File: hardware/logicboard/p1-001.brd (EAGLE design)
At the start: 91 x 90 mm, 70 parts, among them IC1 74LS06N, IC2 4066N, J1 MKR, J2 GPIO, J3 Vcc, J4 RLY, J42 RLY2, J5 SPI, J6 LED, J7 DIN5, J8 DIN5, J9 DIN5, K1 G5V1, Q1 220mA/50V/3.5Ω, Q2 220mA/50V/3.5Ω, T1 2SC1815, U1 DS18B20

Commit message: Removed many parts.
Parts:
- removed A, B: (no value), wirepad:SMD1,27-2,54
- removed C1: 22u, rcl:C025-050X050
- removed C11, C4: 100n, rcl:C025-024X044
- removed C12, C13, C3: 1u, rcl:C050-024X044
- removed C2: 470n, rcl:C050-024X044
- removed D1: (no value), SparkFun-DiscreteSemi:DIODE-1N4148
- removed F1: 1.8A, fuse:TE5
- removed H1, H2: STAND-OFF, SparkFun-Hardware:STAND-OFF
- removed IC1: 74LS06N, 74xx-us:DIL14
- removed IC2: 4066N, 40xx:DIL14
- removed J1: MKR, SparkFun-Connectors:JST-5-PTH
- removed J2: GPIO, SparkFun-Connectors:JST-3-PTH
- removed J3: Vcc, SparkFun-Connectors:JST-2-PTH
- removed J4: RLY, SparkFun-Connectors:JST-2-SMD
- removed J5: SPI, SparkFun-Connectors:JST-5-PTH-VERT
- removed J8, J9: DIN5, SparkFun-Connectors:DIN5-RA-PTH
- removed JP1: PWRSEL, pinhead:2X03
- removed JP2: RTC, SparkFun-Connectors:1X05
- removed JP4: RLYJMP, pinhead:1X02
- removed JP5: PWR, pinhead:1X03
- removed JP7: MNTR, pinhead:1X04
- removed LCD1: AQM0802A-RN-GBW, AQM0802A-RN-GBW:AQM0802A-RN-GBW-FOOTPRINT
- removed Q1, Q2: 220mA/50V/3.5Ω, SparkFun-DiscreteSemi:SOT23-3
- removed R101, R102, R103, R104: 10k, rcl:M2012
- removed RN1: 10k, resistor-net:RN-5
- removed RZ1**, RZ2**, VCCBRIDGE**: Inf, rcl:M2012
- removed SV1: (no value), con-ml:ML16L
- removed U1: DS18B20, SparkFun-Sensors:TO-92-AMMO
- removed V1: 5V, v-reg:78XXL
- removed VDDBRIDGE: 0, rcl:M2012
- moved SV3 13.0 mm to (55.5, 11.0)
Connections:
- removed net ANLG0R: IC2.2, SV1.3
- removed net ANLG1R: IC2.3, SV1.7
- removed net ANLG2R: IC2.9, SV1.11
- removed net ANLG3R: IC2.10, SV1.15
- removed net CAP1N: C12.2, LCD1.3
- removed net CAP1P: C12.1, LCD1.4
- removed net LCDVOUT: C13.2, LCD1.2
- removed net MO2RTN: RN4.9
- removed net MO2SND: RN4.10
- removed net MORTN: J9.5, RN4.13
- removed net MOSND: J9.4, RN4.14
- removed net MTRTN: J8.5, RN4.11
- removed net MTSND: J8.4, RN4.12
- removed net N$1: IC1.8, RN4.6
- removed net N$2: IC1.10, RN4.4
- removed net N$6: IC1.12, RN4.8
- removed net RLYOUT: J4.2, J42.1, K1.10
- removed net SCL: J1.3, Q1.3, R101.1, RZ1**.1
- removed net SDA3V: LCD1.7, Q2.2, R104.1, RZ2**.2
- removed net V+: C1.1, C2.1, D1.C, J0.3, JP1.1, JP5.3, V1.IN
- removed net VCC/VDD: C11.1, C13.1, LCD1.5, LCD1.9, VCCBRIDGE**.1, VDDBRIDGE.1
- removed net VOUT: F1.2, JP1.4, JP1.6
- removed net VOUTRAW: B.1, C3.1, C4.1, D1.A, J4.1, J42.2, JP4.2, K1.5, K1.6, V1.OUT
- removed net VOUTRAW2: A.1, F1.1, JP4.1, K1.1
- new net RLYOUT1: J42.1, K1.10
- new net RLYOUT2: J42.2, K1.5, K1.6
- net ANLG0: no longer IC2.1, RN1.2
- net ANLG1: no longer IC2.4, RN1.3
- net ANLG2: no longer IC2.8, RN1.4
- net ANLG3: no longer IC2.11, RN1.5
- net D7GATE: no longer IC2.12, IC2.13, IC2.5, IC2.6, J1.4
- net DTCT0: no longer SV1.2
- net DTCT1: no longer SV1.6
- net DTCT2: no longer SV1.10
- net DTCT3: no longer SV1.14
- net GND: no longer C1.2, C11.2, C2.2, C3.2, C4.2, IC1.7, IC2.7, J1.1, J2.1, J3.1, J5.1, J8.2, J9.2, JP2.2, JP5.1, JP7.1, LCD1.6, RN1.1, SV1.1, SV1.13, SV1.5, SV1.9, U1.1, V1.GND
- net GPIO0: no longer J2.2
- net GPIO1: no longer J2.3
- net MISO: no longer J5.5
- net MOSI: no longer J5.4
- net NMO2RTN: no longer IC1.13, IC1.6
- net NMORTN: no longer IC1.11, IC1.4
- net NMTRTN: no longer IC1.2, IC1.9
- net RX: no longer IC1.1
- net SCK: no longer J5.3
- net SCL3V: no longer JP2.4, JP7.3, LCD1.8, Q1.2, R102.1, RZ1**.2
- net SDA: no longer J1.2, JP2.5, JP7.4, Q2.3, R103.1, RZ2**.1
- net THS: no longer U1.2
- net TX: no longer IC1.3, IC1.5
- net VCC: no longer IC1.14, IC2.14, J1.5, J3.2, J5.2, JP1.3, JP2.1, JP5.2, JP7.2, R101.2, R103.2, RN4.3, RN4.5, RN4.7, U1.3, VCCBRIDGE**.2
- net VCC/2: no longer JP1.5, SV1.12, SV1.16, SV1.4, SV1.8
- net VDD: no longer Q1.1, Q2.1, R102.2, R104.2, VDDBRIDGE.2
- net VIN: now also J0.3; no longer JP1.2
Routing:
- net GND: track 402.0 -> 0.00 mm, vias 1 -> 0
- net VCC: track 363.1 -> 0.00 mm, vias 7 -> 0
- net SCL3V: track 181.6 -> 0.00 mm, vias 7 -> 0
- net V+: track 181.2 -> 0.00 mm, vias 4 -> 0
- net SDA: track 177.0 -> 0.00 mm, vias 5 -> 0
- net VCC/2: track 138.6 -> 0.00 mm, vias 5 -> 0
- net VOUTRAW: track 129.0 -> 0.00 mm, vias 5 -> 0
- net VDD: track 126.5 -> 0.00 mm, vias 7 -> 0
- net GPIO1: track 125.6 -> 0.00 mm, vias 1 -> 0
- net RX: track 124.8 -> 0.00 mm, vias 2 -> 0
- net RLYOUT: track 114.4 -> 0.00 mm, vias 1 -> 0
- net THS: track 112.9 -> 0.00 mm
- net VIN: track 106.0 -> 0.00 mm, vias 3 -> 0
- net D7GATE: track 102.5 -> 0.00 mm, vias 5 -> 0
- net ANLG2: track 99.5 -> 0.00 mm, vias 7 -> 0
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- removed copper zone on layer 1, net GND
- removed copper zone on layer 16, net GND
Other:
- board text added: "1.0.0-X"
- board text added: "Designed for Takachi PF10-4-7"
- board text added: "Pineapple I"
- board text removed: "+9V"
- board text removed: "1u"
- board text removed: "2.6.1-B"
- board text removed: "22u"
- board text removed: "4066"
- board text removed: "470n"
- board text removed: "5V"
- board text removed: "7406"
- board text removed: "9"
- board text removed: "Adafruit SSD1306"
- board text removed: "Akizuki AQM0802A-RN-GBW"
- board text removed: "C"
- board text removed: "DISP"
- board text removed: "Designed for Takachi PF10-4-10"
- board text removed: "GND"
- board text removed: "GPIO"
- board text removed: "GeekPort II"
- board text removed: "I"
- board text removed: "MKR"
- board text removed: "NC"
- board text removed: "O"
- board text removed: "Pineapple IIb"
- board text removed: "RTC"
- board text removed: "SCL"
- board text removed: "SDA"
- board text removed: "SPI"
- board text removed: "SparkFun Real Time Clock Module (12708)"
- board text removed: "THS*"
- board text removed: "V+"
- board text removed: "Vcc"
- board text removed: "Vcc/2"
- board text removed: "Vin"
- board text removed: "Vout"

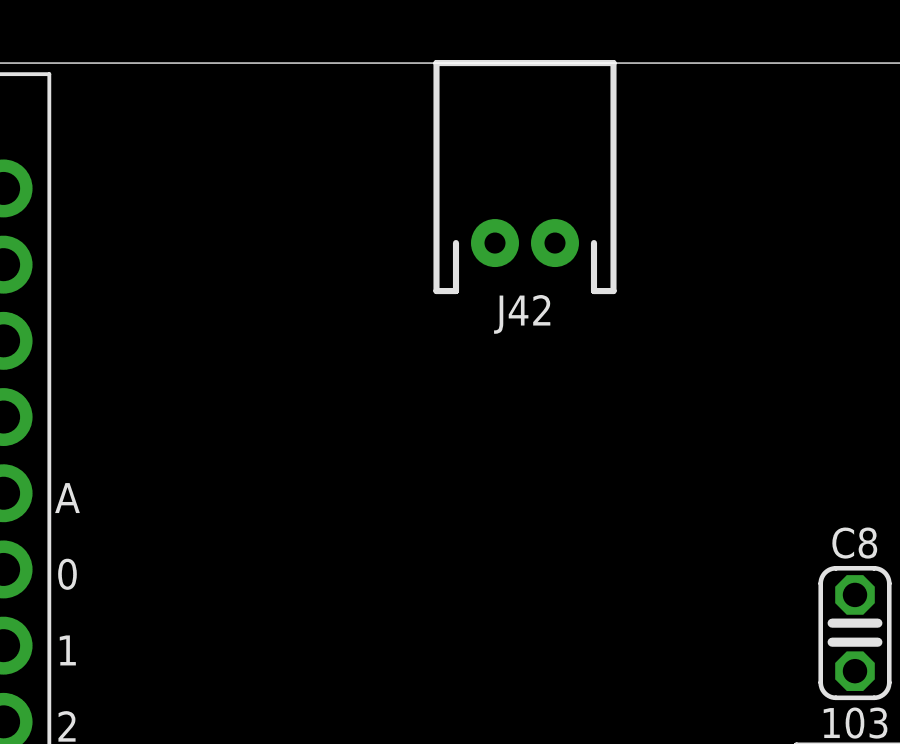
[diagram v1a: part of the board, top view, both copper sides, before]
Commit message: 3-pin relay port.
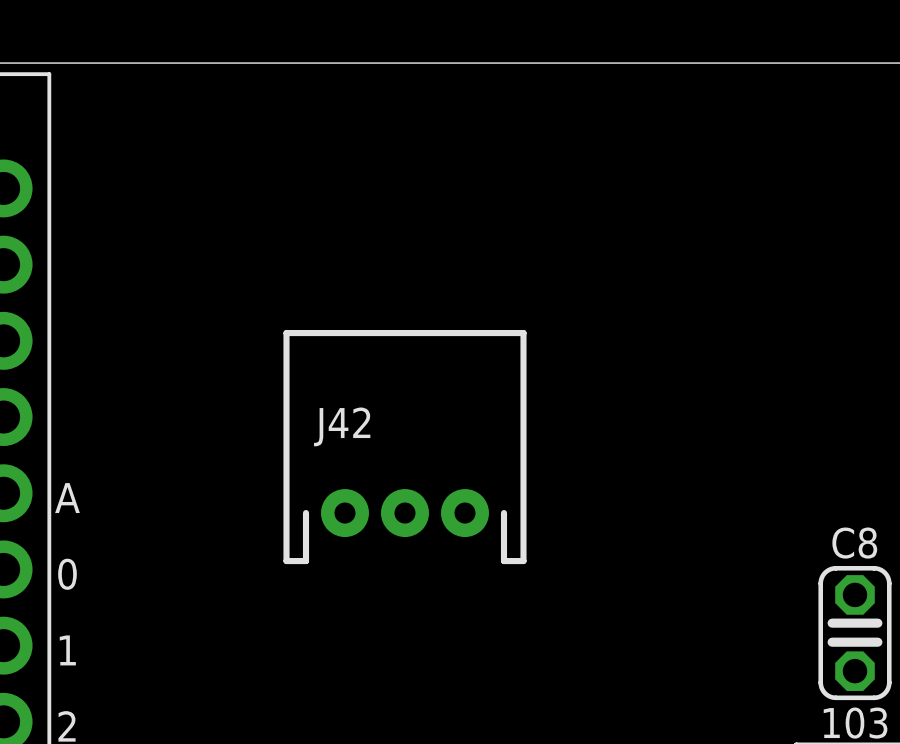
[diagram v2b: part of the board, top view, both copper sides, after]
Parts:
- J42: value RLY2 -> (none); device SparkFun-Connectors:JST-2-PTH -> SparkFun-Connectors:JST-3-PTH
- moved J42 9.85 mm to (58.0, 75.0)
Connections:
- new net RLYOUT3: J42.3, K1.1
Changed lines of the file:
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@@
 <attribute name="VALUE" x="46.61" y="6.555" size="1.27" layer="27"/>
 </element>
-<element name="J42" library="SparkFun-Connectors" library_urn="urn:adsk.eagle:library:513" package="JST-2-PTH" package3d_urn="urn:adsk.eagle:package:38053/1" value="RLY2" x="62" y="84" smashed="yes">
-<attribute name="NAME" x="62" y="81.75" size="1" layer="25" ratio="20" align="center"/>
-<attribute name="PROD_ID" value="CONN-09863" x="62" y="84" size="1.778" layer="27" display="off"/>
-<attribute name="SKU" value="PRT-09914" x="62" y="84" size="1.778" layer="27" display="off"/>
-<attribute name="VALUE" x="60.73" y="86.73" size="0.6096" layer="27" font="vector" ratio="20"/>
+<element name="J42" library="SparkFun-Connectors" library_urn="urn:adsk.eagle:library:513" package="JST-3-PTH" package3d_urn="urn:adsk.eagle:package:38069/1" value="" x="58" y="75" smashed="yes">
+<attribute name="NAME" x="56" y="78" size="1" layer="25" ratio="20" align="center"/>
+<attribute name="PROD_ID" value="WIRE-10037" x="58" y="75" size="1.778" layer="27" display="off"/>
+<attribute name="SF_ID" value="PRT-09915" x="58" y="75" size="1.778" layer="27" display="off"/>
+<attribute name="VALUE" x="56.349" y="77.54" size="0.6096" layer="27" font="vector" ratio="20"/>
 </element>
 </elements>
@@
 <contactref element="K1" pad="10"/>
 <contactref element="J42" pad="1"/>
-<wire x1="10.92" y1="42.54" x2="61" y2="84" width="0" layer="19" extent="1-1"/>
+<wire x1="56" y1="75" x2="10.92" y2="42.54" width="0" layer="19" extent="1-1"/>
 </signal>
 <signal name="MISO">
@@
 <contactref element="K1" pad="5"/>
 <contactref element="J42" pad="2"/>
-<wire x1="21.08" y1="42.54" x2="63" y2="84" width="0" layer="19" extent="1-1"/>
 <wire x1="21.08" y1="37.46" x2="21.08" y2="42.54" width="0" layer="19" extent="1-1"/>
+<wire x1="58" y1="75" x2="21.08" y2="37.46" width="0" layer="19" extent="1-1"/>
 </signal>
 <signal name="N$1" class="2">
 </signal>
+<signal name="RLYOUT3">
+<contactref element="K1" pad="1"/>
+<contactref element="J42" pad="3"/>
+<wire x1="60" y1="75" x2="10.92" y2="37.46" width="0" layer="19" extent="1-1"/>
+</signal>
 </signals>

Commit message: Removed many parts.
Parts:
- removed J6: LED, SparkFun-Connectors:JST-3-PTH-VERT
- moved C7 56.3 mm to (43.0, 3.50)
- moved RN2 55.1 mm to (9.50, 18.0)
- moved RN3 48.1 mm to (10.5, 22.0)
- moved RN4 40.6 mm to (66.0, 7.00)
- moved MC1 33.5 mm to (45.0, 33.0)
- moved J0 33.0 mm to (22.5, 46.0)
- moved LOGO1 33.0 mm to (7.00, 35.0)
- moved U$1 33.0 mm to (7.00, 40.0)
- moved SV3 30.1 mm to (80.0, 28.5), turned to 90 degrees
- moved R5 30.1 mm to (50.0, 6.50)
- moved R4 30.0 mm to (49.0, 3.50)
- moved C8 27.2 mm to (57.0, 49.0)
- moved C9 27.2 mm to (60.5, 49.0)
- moved J42 26.0 mm to (68.0, 51.0)
- moved R3 23.3 mm to (52.0, 7.50)
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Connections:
- net GND: no longer J6.2
- net LED0A: no longer J6.3
- net LED1A: no longer J6.1
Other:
- board size 91 x 90 mm -> 91 x 57 mm
- board text removed: "*"
- board text removed: "0"
- board text removed: "2-472"
- board text removed: "3"
- board text removed: "A"
- board text removed: "Arduino Only"
- board text removed: "Direct 5V"
- board text removed: "Dual Regulator"
- board text removed: "I/O"
- board text removed: "OUT"
- board text removed: "OUT2"
- board text removed: "Single Regulator"
- board text removed: "THRU"
- board text removed: "USB"

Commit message: Removed several parts.
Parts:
- removed C10: 100n, rcl:C025-024X044
- removed R3: 1k, resistor:0204/5
- removed RN2, RN3: 4.7k, resistor-net:RN-5
- removed RN4: 220, resistor-dil:DIL16
- added RA: 220, resistor:0204/5
- added RB: 4.7k, resistor:0204/5
- moved K1 50.6 mm to (62.0, 22.0)
- moved C6 49.2 mm to (19.0, 26.0)
- moved R4 48.6 mm to (68.5, 48.0)
- moved C9 45.5 mm to (75.5, 6.00)
- moved C8 45.2 mm to (71.0, 6.00)
- moved R5 42.7 mm to (68.5, 45.0)
- moved D2 39.8 mm to (62.0, 9.00)
- moved R2 38.9 mm to (64.0, 12.0)
- moved D3 38.9 mm to (33.0, 26.0)
- moved T1 36.1 mm to (58.0, 14.0)
- moved OK1 36.0 mm to (26.0, 26.0)
- moved R1 34.8 mm to (64.0, 16.0)
- moved C5 34.7 mm to (45.5, 7.00)
- moved C7 29.0 mm to (70.0, 14.0)
- moved J42 0.50 mm to (68.5, 51.0)
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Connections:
- removed net MNTRA: OK1.4, RN4.16
- removed net NMO2RTN: RN2.5
- removed net NMORTN: RN2.4
- removed net NMTRTN: RN2.3
- removed net SCL3V: MC1.P$10, RN3.3, SV3.9
- removed net VCC/2: R3.2, RN4.1
- new net SCL: MC1.P$10, SV3.9
- net AREF: no longer C10.1, R3.1
- net GND: now also OK1.4; no longer C10.2
- net MIDIINSND: now also RA.1; no longer RN4.2
- net MISND: now also RA.2; no longer RN4.15
- net MNTR: no longer RN3.5
- net RX: now also RB.1; no longer RN2.2
- net SDA: no longer RN3.2
- net THS: no longer RN3.4
- net VCC: now also RB.2; no longer RN2.1, RN3.1
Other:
- board text removed: "00"
- board text removed: "01"
- board text removed: "02"
- board text removed: "03"
- board text removed: "1"
- board text removed: "102"
- board text removed: "104"
- board text removed: "2"
- board text removed: "221"
- board text removed: "4"
- board text removed: "473"
- board text removed: "5"
- board text removed: "D7"
- board text removed: "G"
- board text removed: "G0"
- board text removed: "G1"
- board text removed: "L0"
- board text removed: "L1"
- board text removed: "LED00"
- board text removed: "LTC1485 OR MAX3468"
- board text removed: "MC1"
- board text removed: "RX"
- board text removed: "SC"
- board text removed: "SD"
- board text removed: "TH"
- board text removed: "TX"
- board text removed: "V"

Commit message: Removed many parts.
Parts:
- moved U$1 11.7 mm to (9.00, 28.5), turned to 90 degrees
- moved LOGO1 7.63 mm to (3.00, 28.5), turned to 90 degrees
- moved C6 2.50 mm to (19.0, 28.5)
- moved D3 2.50 mm to (33.0, 28.5)
- moved OK1 2.50 mm to (26.0, 28.5)
- moved RA 2.50 mm to (16.0, 28.5)
- moved RB 2.50 mm to (13.0, 28.5)
- moved JP6 1.41 mm to (76.0, 52.0)
- renumbered J42 to J4

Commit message: The first should-be-working model.
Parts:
- added D2B, D2C: (no value), SparkFun-DiscreteSemi:DIODE-1N4148
- added J4B, J4C: (no value), SparkFun-Connectors:JST-3-PTH
- added K1B, K1C: G5V1, relay:G5V1
- added R1B, R1C: 1k, resistor:0204/5
- added R2B, R2C: 47k, resistor:0204/5
- added T1B, T1C: 2SC1815, transistor:TO92-ECB
- moved C9 40.0 mm to (58.0, 42.0)
- moved C8 24.7 mm to (58.0, 27.0)
- moved C7 12.2 mm to (58.0, 12.0)
- moved K1 11.2 mm to (67.0, 12.0)
- moved R1 10.0 mm to (63.0, 6.00)
- moved R5 9.96 mm to (59.0, 48.0)
- moved R2 9.22 mm to (71.0, 6.00)
- moved T1 9.00 mm to (58.0, 5.00)
- moved D2 7.81 mm to (67.0, 3.00), turned to 0 degrees
- moved SV3 4.00 mm to (84.0, 28.5)
- moved J4 0.50 mm to (68.0, 51.0)
- moved R4 0.50 mm to (68.0, 48.0)
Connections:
- new net RLYDRV1: R1B.1, R2B.2, T1B.B
- new net RLYDRV2: R1C.1, R2C.2, T1C.B
- new net RLYOUT1B: J4B.1, K1B.10
- new net RLYOUT1C: J4C.1, K1C.10
- new net RLYOUT2B: J4B.2, K1B.5, K1B.6
- new net RLYOUT2C: J4C.2, K1C.5, K1C.6
- new net RLYOUT3A: J4B.3
- new net RLYOUT3B: K1B.1
- new net RLYOUT3C: J4C.3, K1C.1
- new net RLYSNK1: D2B.A, K1B.9, T1B.C
- new net RLYSNK2: D2C.A, K1C.9, T1C.C
- net GND: now also R2B.1, R2C.1, T1B.E, T1C.E
- net GPIO0: now also R1B.2
- net GPIO1: now also R1C.2
- net VCC: now also D2B.C, D2C.C, K1B.2, K1C.2
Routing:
- net GND: track 0.00 -> 255.3 mm, vias 0 -> 1
- net VCC: track 0.00 -> 166.3 mm, vias 0 -> 2
- net RX: track 0.00 -> 96.6 mm
- net RLYOUT3: track 0.00 -> 63.7 mm, vias 0 -> 1
- net RLYOUT1: track 0.00 -> 58.8 mm, vias 0 -> 1
- net GPIO1: track 0.00 -> 58.2 mm
- net RLYOUT2C: track 0.00 -> 57.9 mm, vias 0 -> 1
- net DTCT3: track 0.00 -> 52.1 mm
- net LED0: track 0.00 -> 50.3 mm
- net RLYOUT2: track 0.00 -> 49.9 mm, vias 0 -> 1
- net THS: track 0.00 -> 48.6 mm
- net DTCT1: track 0.00 -> 47.7 mm
- net SCL: track 0.00 -> 45.4 mm, vias 0 -> 1
- net D7GATE: track 0.00 -> 45.0 mm, vias 0 -> 1
- net DTCT2: track 0.00 -> 44.1 mm, vias 0 -> 1
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- added copper zone on layer 1, net GND
- added copper zone on layer 16, net GND

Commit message: Autorouted.
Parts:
- moved R4 1.00 mm to (68.0, 47.0), turned to 180 degrees
- moved R5 1.00 mm to (59.0, 47.0), turned to 180 degrees
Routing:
- net RLYOUT2: track 49.9 -> 77.2 mm, vias 1 -> 0
- net LED0: track 50.3 -> 30.2 mm
- net GND: track 255.3 -> 239.3 mm, vias 1 -> 2
- net DTCT0: track 38.2 -> 52.2 mm
- net VCC: track 166.3 -> 180.1 mm
- net RLYOUT3C: track 33.9 -> 44.3 mm
- net RLYOUT1: track 58.8 -> 69.0 mm, vias 1 -> 0
- net SCL: track 45.4 -> 35.3 mm
- net D7GATE: track 45.0 -> 35.1 mm
- net RLYOUT2C: track 57.9 -> 50.3 mm
- net DTCT3: track 52.1 -> 47.2 mm
- net LED1A: track 20.1 -> 15.5 mm
- net LED1: track 9.56 -> 5.21 mm
- net RLYOUT2B: track 38.4 -> 34.5 mm, vias 1 -> 0
- net LED0A: track 13.3 -> 9.80 mm
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- removed copper zone on layer 1, net GND
- removed copper zone on layer 16, net GND

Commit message: Silk.
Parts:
- removed RA: 220, resistor:0204/5
- removed RB: 4.7k, resistor:0204/5
- added R1A: 1k, resistor:0204/5
- added R2A: 47k, resistor:0204/5
- R1: value 1k -> 220
- R2: value 47k -> 4.7k
- moved R2 62.2 mm to (13.0, 28.5), turned to 90 degrees
- moved R1 52.1 mm to (16.0, 28.5), turned to 90 degrees
- renumbered C7 to C7A, C8 to C7B, C9 to C7C, D2 to D2A, J4 to J4A, K1 to K1A, T1 to T1A
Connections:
- net GND: now also R2A.1; no longer R2.1
- net MIDIINSND: now also R1.1; no longer RA.1
- net MISND: now also R1.2; no longer RA.2
- net RLY: now also R1A.2; no longer R1.2
- net RLYDRV: now also R1A.1, R2A.2; no longer R1.1, R2.2
- net RX: now also R2.1; no longer RB.1
- net VCC: now also R2.2; no longer RB.2
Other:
- board text added: "102"
- board text added: "221"
- board text added: "472"
- board text added: "A"
- board text added: "B"
- board text added: "C"
- board text added: "GPIO0 (D5)"
- board text added: "GPIO1 (D8)"
- board text added: "RLY (D4)"
- board text added: "TLP2630"
